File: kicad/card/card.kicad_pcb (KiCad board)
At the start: 2 copper layers, 30 x 34 mm, 6 parts, among them U1 RP2350_60QFN, U2 TLV70030_SOT23-5, U3 BNO086

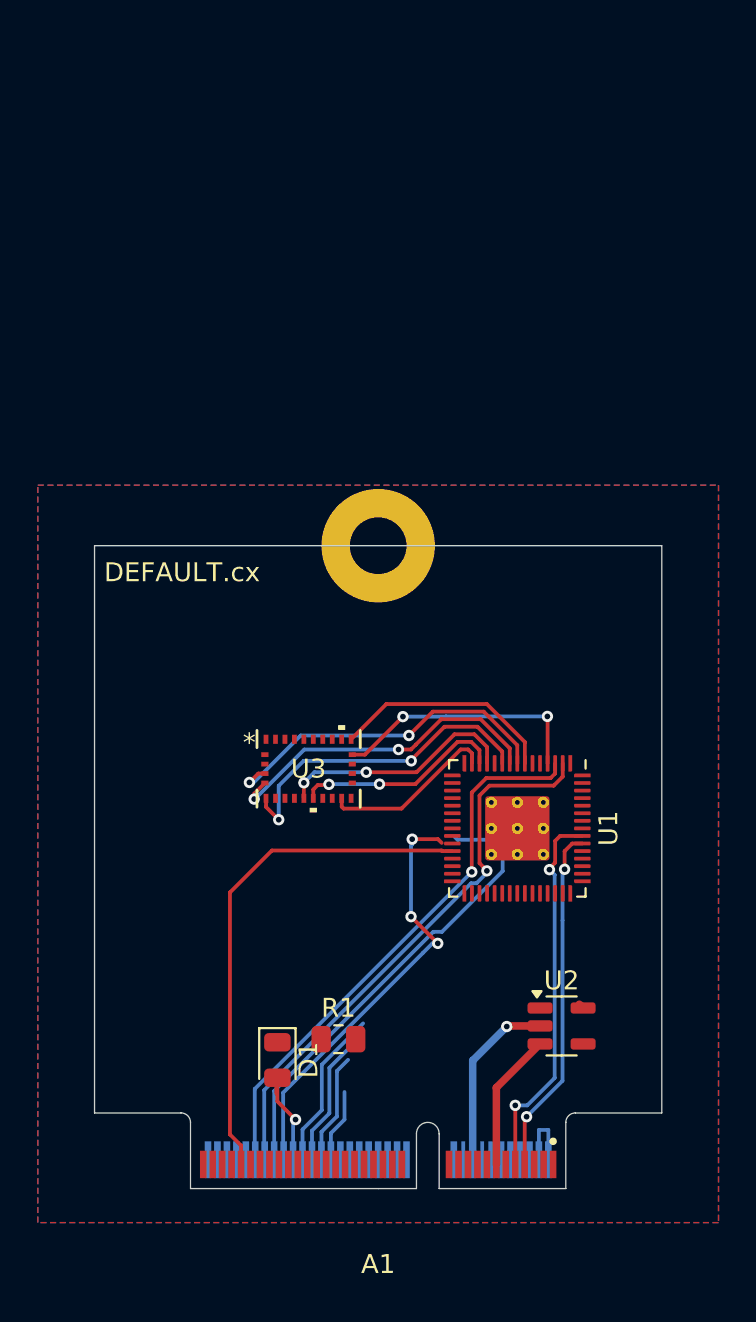
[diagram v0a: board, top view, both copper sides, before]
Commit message: minimal "blink" bring up revised schematic and starting with new components to place
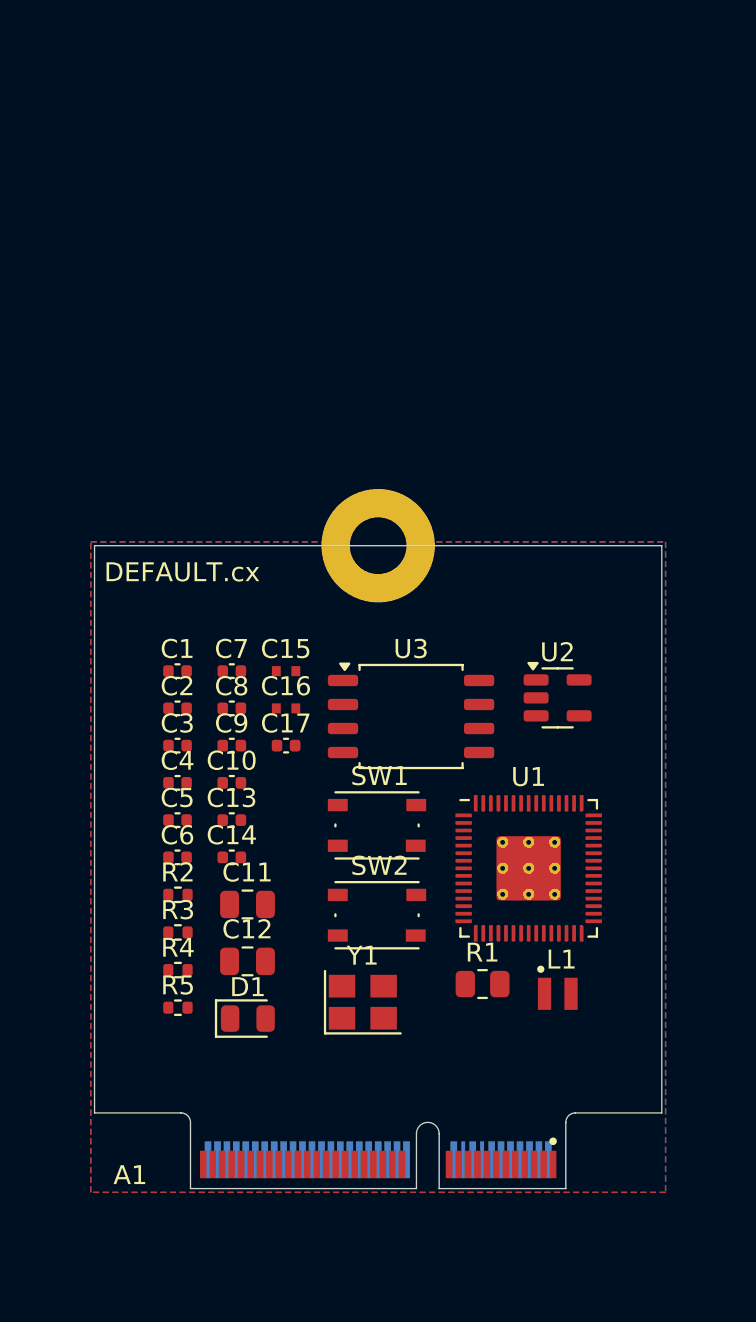
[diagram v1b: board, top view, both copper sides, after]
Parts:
- added C1: 100n, Capacitor_SMD:C_0402_1005Metric, F.Cu at (89.4, 104.8)
- added C10: 100n, Capacitor_SMD:C_0402_1005Metric, F.Cu at (92.3, 110.7)
- added C11: 10u, Capacitor_SMD:C_0805_2012Metric, F.Cu at (93.1, 117.2)
- added C12: 10u, Capacitor_SMD:C_0805_2012Metric, F.Cu at (93.1, 120.2)
- added C13: 15p, Capacitor_SMD:C_0402_1005Metric, F.Cu at (92.3, 112.7)
- added C14: 15p, Capacitor_SMD:C_0402_1005Metric, F.Cu at (92.3, 114.7)
- added C15: 4.7u, RP2350_60QFN_minimal:C_0402_1005Metric_small_pads, F.Cu at (95.1, 104.8)
- added C16: 4.7u, RP2350_60QFN_minimal:C_0402_1005Metric_small_pads, F.Cu at (95.1, 106.8)
- added C17: 4.7u, Capacitor_SMD:C_0402_1005Metric, F.Cu at (95.1, 108.8)
- added C2: 4.7u, Capacitor_SMD:C_0402_1005Metric, F.Cu at (89.4, 106.8)
- added C3: 100n, Capacitor_SMD:C_0402_1005Metric, F.Cu at (89.4, 108.8)
- added C4: 100n, Capacitor_SMD:C_0402_1005Metric, F.Cu at (89.4, 110.7)
- added C5: 100n, Capacitor_SMD:C_0402_1005Metric, F.Cu at (89.4, 112.7)
- added C6: 100n, Capacitor_SMD:C_0402_1005Metric, F.Cu at (89.4, 114.7)
- added C7: 100n, Capacitor_SMD:C_0402_1005Metric, F.Cu at (92.3, 104.8)
- added C8: 100n, Capacitor_SMD:C_0402_1005Metric, F.Cu at (92.3, 106.8)
- added C9: 100n, Capacitor_SMD:C_0402_1005Metric, F.Cu at (92.3, 108.8)
- added L1: 3.3u, RP2350_60QFN_minimal:L_pol_2016, F.Cu at (109.5, 121.9)
- added R2: 1k, Resistor_SMD:R_0402_1005Metric, F.Cu at (89.4, 116.7)
- added R3: 33, Resistor_SMD:R_0402_1005Metric, F.Cu at (89.4, 118.7)
- added R4: 1k, Resistor_SMD:R_0402_1005Metric, F.Cu at (89.4, 120.6)
- added R5: 1k, Resistor_SMD:R_0402_1005Metric, F.Cu at (89.4, 122.6)
- added SW1: SW_Push, Button_Switch_SMD:SW_Push_1P1T_NO_Vertical_Wuerth_434133025816, F.Cu at (99.9, 113.0)
- added SW2: SW_Push, Button_Switch_SMD:SW_Push_1P1T_NO_Vertical_Wuerth_434133025816, F.Cu at (99.9, 117.7)
- added Y1: ABM8-272-T3, Crystal:Crystal_SMD_3225-4Pin_3.2x2.5mm, F.Cu at (99.2, 122.3)
- U3: value BNO086 -> W25Q128JVS; footprint footprints:QFN28_BNO086_CEV -> Package_SO:SOIC-8_5.23x5.23mm_P1.27mm
- moved U2 17.4 mm to (109.5, 106.2)
- moved R1 8.16 mm to (105.5, 121.4)
- moved U3 6.09 mm to (101.7, 107.2)
- moved D1 2.69 mm to (93.1, 123.2), turned to 0 degrees
- moved U1 2.20 mm to (108.0, 115.3), turned to 0 degrees
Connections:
- D1 pad 1: Net-(D1-K) -> GND
- D1 pad 2: Net-(A1-TP90) -> Net-(D1-A)
- R1 pad 1: Net-(D1-K) -> Net-(A1-TP89)
- R1 pad 2: GND -> Net-(D1-A)
- U1 pad 1: unconnected-(U1-IOVDD-Pad1) -> +3V3
- U1 pad 10: Net-(U1-GPIO7) -> unconnected-(U1-GPIO7-Pad10)
- U1 pad 11: unconnected-(U1-IOVDD-Pad11) -> +3V3
- U1 pad 12: Net-(U1-GPIO8) -> unconnected-(U1-GPIO8-Pad12)
- U1 pad 13: Net-(U1-GPIO9) -> unconnected-(U1-GPIO9-Pad13)
- U1 pad 14: Net-(U1-GPIO10) -> unconnected-(U1-GPIO10-Pad14)
- U1 pad 15: Net-(A1-TP87) -> unconnected-(U1-GPIO11-Pad15)
- U1 pad 16: Net-(A1-TP88) -> unconnected-(U1-GPIO12-Pad16)
- U1 pad 17: Net-(A1-TP89) -> unconnected-(U1-GPIO13-Pad17)
- U1 pad 20: unconnected-(U1-IOVDD-Pad20) -> +3V3
- U1 pad 21: unconnected-(U1-XIN-Pad21) -> Net-(U1-XIN)
- U1 pad 22: unconnected-(U1-XOUT-Pad22) -> Net-(U1-XOUT)
- U1 pad 23: unconnected-(U1-DVDD-Pad23) -> +1V1
- U1 pad 24: Net-(A1-TP92) -> Net-(A1-TP85)
- U1 pad 25: Net-(A1-TP91) -> Net-(A1-TP86)
- U1 pad 26: RESET -> Net-(A1-XIO_A)
- U1 pad 30: unconnected-(U1-IOVDD-Pad30) -> +3V3
- U1 pad 38: unconnected-(U1-IOVDD-Pad38) -> +3V3
- U1 pad 39: unconnected-(U1-DVDD-Pad39) -> +1V1
- U1 pad 4: Net-(U1-GPIO2) -> Net-(A1-TP92)
- U1 pad 41: unconnected-(U1-GPIO27_ADC1-Pad41) -> Net-(U1-GPIO27_ADC1)
- U1 pad 42: unconnected-(U1-GPIO28_ADC2-Pad42) -> Net-(A1-TP88)
- U1 pad 43: unconnected-(U1-GPIO29_ADC3-Pad43) -> Net-(A1-TP87)
- U1 pad 44: unconnected-(U1-ADC_AVDD-Pad44) -> +3V3
- U1 pad 45: unconnected-(U1-IOVDD-Pad45) -> +3V3
- U1 pad 46: +3.3V -> Net-(U1-VREG_AVDD)
- U1 pad 47: +3.3V -> GND
- U1 pad 48: +3.3V -> Net-(U1-VREG_LX)
- U1 pad 49: +3.3V -> +3V3
- U1 pad 5: Net-(U1-GPIO3) -> Net-(A1-TP91)
- U1 pad 50: +3.3V -> +1V1
- U1 pad 51: Net-(A1-USB_DM) -> Net-(U1-USB_DM)
- U1 pad 52: Net-(A1-USB_DP) -> Net-(U1-USB_DP)
- U1 pad 53: unconnected-(U1-USB_OTP_VDD-Pad53) -> +3V3
- U1 pad 54: unconnected-(U1-QSPI_IOVDD-Pad54) -> +3V3
- U1 pad 55: unconnected-(U1-QSPI_SD3-Pad55) -> Net-(U1-QSPI_SD3)
- U1 pad 56: unconnected-(U1-QSPI_SCLK-Pad56) -> Net-(U1-QSPI_SCLK)
- U1 pad 57: unconnected-(U1-QSPI_SD0-Pad57) -> Net-(U1-QSPI_SD0)
- U1 pad 58: unconnected-(U1-QSPI_SD2-Pad58) -> Net-(U1-QSPI_SD2)
- U1 pad 59: unconnected-(U1-QSPI_SD1-Pad59) -> Net-(U1-QSPI_SD1)
- U1 pad 6: unconnected-(U1-DVDD-Pad6) -> +1V1
- U1 pad 60: unconnected-(U1-QSPI_SS-Pad60) -> Net-(U1-QSPI_SS)
- U1 pad 7: Net-(U1-GPIO4) -> Net-(A1-TP90)
- U1 pad 8: Net-(U1-GPIO5) -> Net-(A1-TP89)
- U1 pad 9: Net-(U1-GPIO6) -> unconnected-(U1-GPIO6-Pad9)
- U2 pad 1: +5V -> Net-(JP1-B)
- U2 pad 2: GND -> Net-(U2-GND)
- U2 pad 3: +5V -> Net-(JP1-B)
- U3 pad 1: unconnected-(U3-RESV_NC-Pad1) -> Net-(U1-QSPI_SS)
- U3 pad 2: unconnected-(U3-GND-Pad2) -> Net-(U1-QSPI_SD1)
- U3 pad 3: unconnected-(U3-VDD-Pad3) -> Net-(U1-QSPI_SD2)
- U3 pad 4: Net-(U1-GPIO5) -> GND
- U3 pad 5: Net-(U1-GPIO6) -> Net-(U1-QSPI_SD0)
- U3 pad 6: Net-(U1-GPIO7) -> Net-(U1-QSPI_SCLK)
- U3 pad 7: unconnected-(U3-RESV_NC-Pad7) -> Net-(U1-QSPI_SD3)
- U3 pad 8: unconnected-(U3-RESV_NC-Pad8) -> +3V3
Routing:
- net Net-(A1-UART_TX): track 30.3 -> 0.00 mm, vias 1 -> 0
- net Net-(A1-UART_RX): track 29.2 -> 0.00 mm, vias 1 -> 0
- net RESET: track 27.3 -> 0.00 mm
- net Net-(A1-TP92): track 24.5 -> 0.00 mm
- net Net-(A1-TP91): track 22.8 -> 0.00 mm, vias 3 -> 0
- net Net-(A1-USB_DP): track 20.1 -> 0.00 mm, vias 2 -> 0
- net Net-(U1-GPIO5): track 18.6 -> 0.00 mm, vias 2 -> 0
- net Net-(A1-USB_DM): track 18.6 -> 0.00 mm, vias 2 -> 0
- net Net-(U1-GPIO6): track 17.8 -> 0.00 mm, vias 2 -> 0
- net Net-(U1-GPIO7): track 17.7 -> 0.00 mm, vias 2 -> 0
- net Net-(A1-TP90): track 14.2 -> 0.00 mm, vias 1 -> 0
- net Net-(U1-GPIO2): track 13.6 -> 0.00 mm, vias 2 -> 0
- net Net-(U1-GPIO8): track 12.7 -> 0.00 mm, vias 2 -> 0
- net Net-(U1-GPIO4): track 11.9 -> 0.00 mm
- net Net-(U1-GPIO9): track 11.3 -> 0.00 mm, vias 2 -> 0
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
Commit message: compentents positioned in lower half of PCB
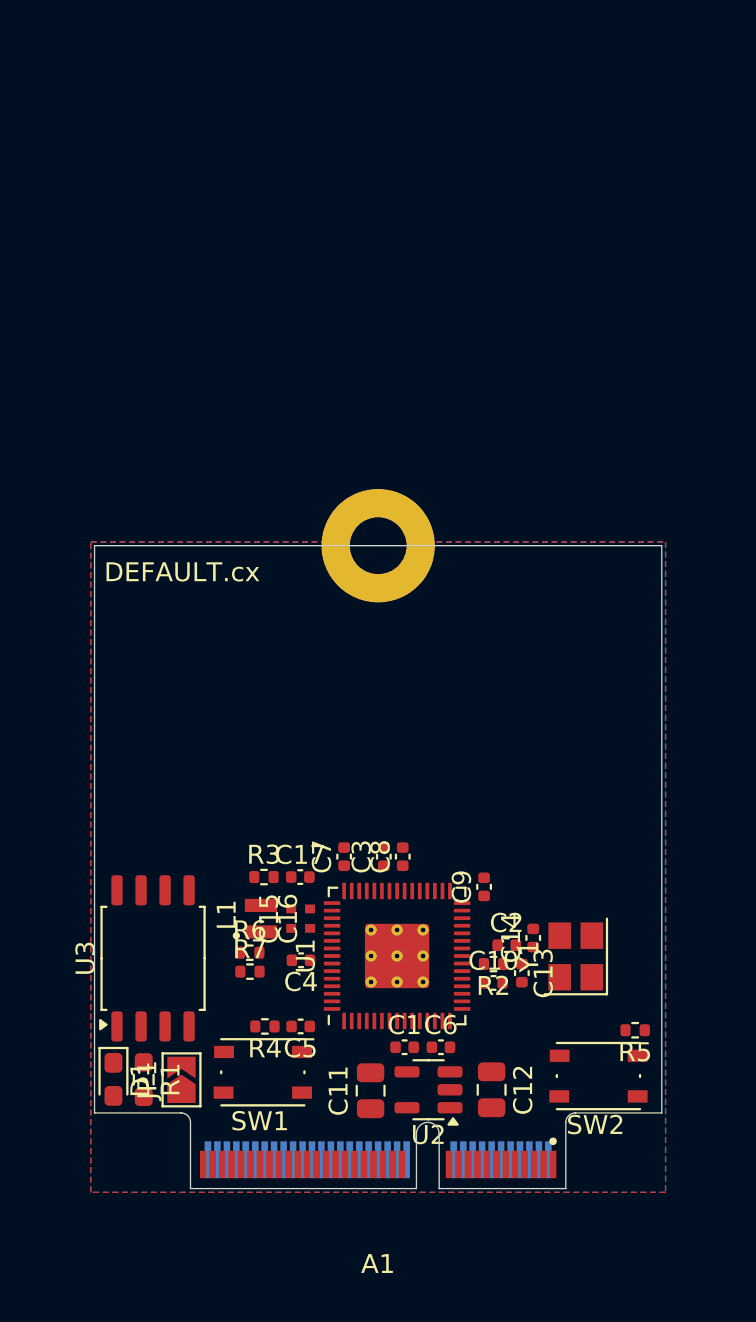
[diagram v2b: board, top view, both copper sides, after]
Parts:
- added JP1: Alt 5v, Jumper:SolderJumper-2_P1.3mm_Open_TrianglePad1.0x1.5mm, F.Cu at (89.6, 126.5)
- added R6: 27Ω, Resistor_SMD:R_0402_1005Metric, F.Cu at (93.2, 119.7)
- added R7: 27Ω, Resistor_SMD:R_0402_1005Metric, F.Cu at (93.2, 120.7)
- D1: footprint LED_SMD:LED_0805_2012Metric -> LED_SMD:LED_0603_1608Metric_Pad1.05x0.95mm_HandSolder
- R1: footprint Resistor_SMD:R_0805_2012Metric -> Resistor_SMD:R_0603_1608Metric_Pad0.98x0.95mm_HandSolder
- SW1: value SW_Push -> USB_BOOT
- SW2: value SW_Push -> RESET
- U1: value RP2350_60QFN -> RP2350A
- U3: value W25Q128JVS -> W25Q128
- Y1: value ABM8-272-T3 -> 12MHz
- moved R5 24.2 mm to (113.6, 123.8), turned to 180 degrees
- moved C1 23.2 mm to (101.4, 124.7)
- moved U2 21.8 mm to (102.7, 127.0), turned to 180 degrees
- moved C2 21.4 mm to (106.8, 119.3)
- moved U3 18.7 mm to (88.1, 120.0), turned to 90 degrees
- moved R1 18.6 mm to (87.6, 126.4), turned to -90 degrees
- moved C10 17.4 mm to (106.1, 121.3)
- moved C13 17.3 mm to (107.6, 120.8), turned to -90 degrees
- moved C6 17.2 mm to (103.3, 124.7)
- moved R2 17.1 mm to (106.1, 120.3), turned to 180 degrees
- moved C14 16.5 mm to (108.2, 118.9), turned to 90 degrees
- moved L1 16.2 mm to (93.8, 117.9), turned to 90 degrees
- moved C9 15.3 mm to (105.6, 116.2), turned to 90 degrees
- moved C12 14.6 mm to (106.0, 127.0), turned to -90 degrees
- moved SW2 14.5 mm to (111.7, 126.2), turned to 180 degrees
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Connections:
- A1 pad 13: +5V -> Net-(JP1-B)
- A1 pad 18: GND -> unconnected-(A1-GND-Pad18)
- A1 pad 2: +3.3V -> Net-(U1-GPIO27_ADC1)
- A1 pad 38: unconnected-(A1-TP85-Pad38) -> Net-(A1-TP85)
- A1 pad 4: +3.3V -> Net-(U1-GPIO27_ADC1)
- A1 pad 46: unconnected-(A1-TP86-Pad46) -> Net-(A1-TP86)
- A1 pad 52: Net-(A1-TP89) -> unconnected-(A1-TP89-Pad52)
- A1 pad 54: Net-(A1-TP90) -> Net-(A1-XIO_B)
- A1 pad 67: RESET -> Net-(A1-XIO_A)
- A1 pad 68: +5V -> Net-(JP1-A)
- A1 pad 70: +5V -> Net-(JP1-A)
- A1 pad 71: GND -> Net-(A1-GND-Pad71)
- A1 pad 72: +5V -> Net-(JP1-A)
- A1 pad 73: GND -> Net-(A1-GND-Pad71)
- R1 pad 1: Net-(A1-TP89) -> Net-(A1-XIO_B)
- U1 pad 8: Net-(A1-TP89) -> Net-(A1-XIO_B)

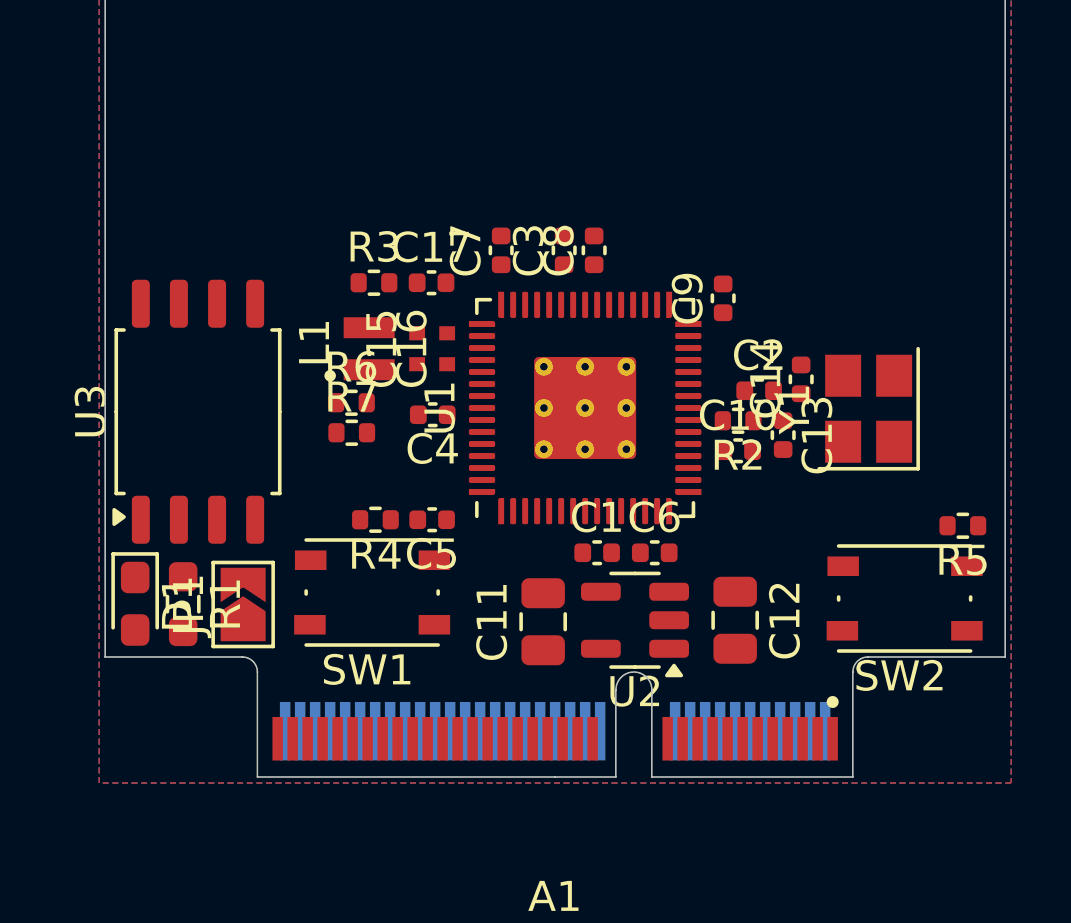
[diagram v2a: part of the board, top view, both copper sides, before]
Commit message: mostly routed, USB & +5V alt?
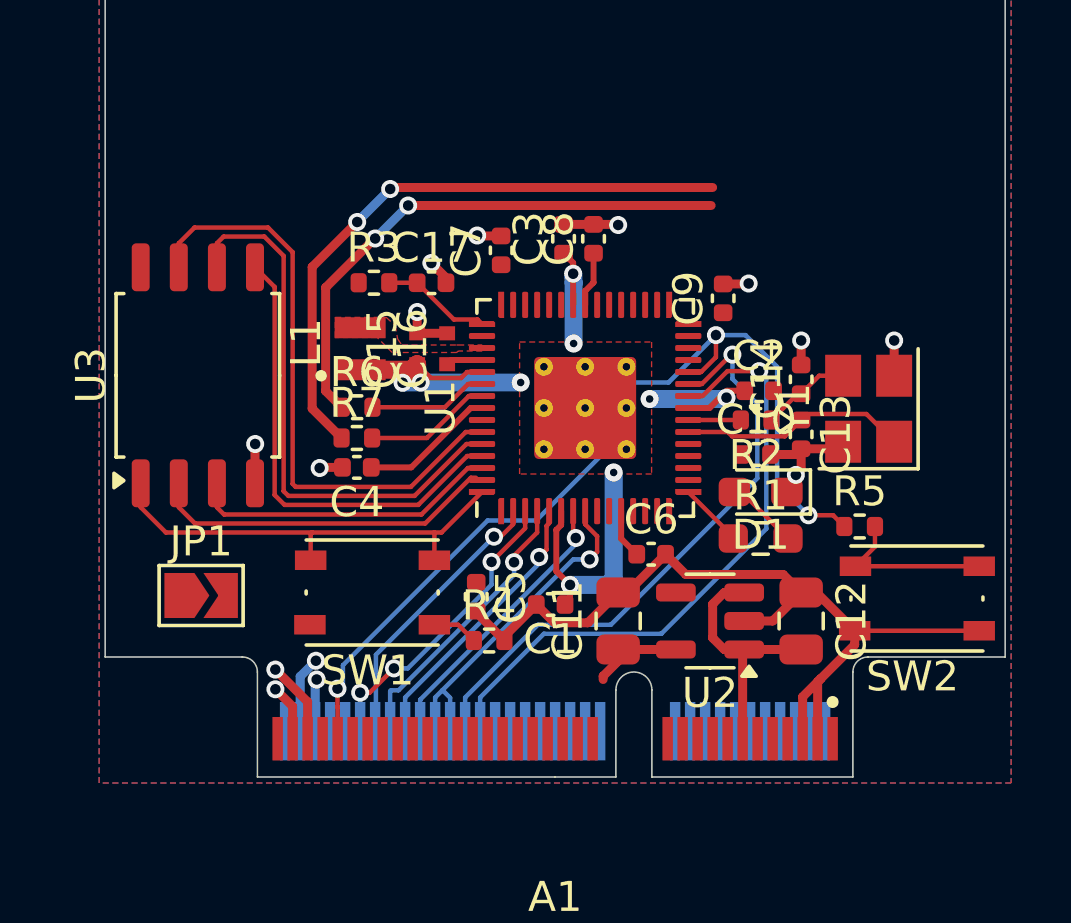
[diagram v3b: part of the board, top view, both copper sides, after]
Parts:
- moved D1 21.2 mm to (106.8, 122.7), turned to 180 degrees
- moved R1 19.4 mm to (106.8, 124.2), turned to 0 degrees
- moved R4 5.53 mm to (97.8, 127.7), turned to 0 degrees
- moved R5 3.44 mm to (110.2, 123.8), turned to 0 degrees
- moved C4 3.08 mm to (93.4, 121.9)
- moved C5 2.96 mm to (97.4, 126.2), turned to -90 degrees
- moved C11 2.50 mm to (102.1, 127.0)
- moved U2 2.50 mm to (105.2, 127.0)
- moved C1 2.32 mm to (99.8, 126.5), turned to 180 degrees
- moved C12 2.20 mm to (108.2, 127.0)
- moved JP1 1.43 mm to (88.2, 126.2), turned to 0 degrees
- moved U3 1.22 mm to (88.1, 118.8)
- moved C10 0.61 mm to (106.7, 121.5)
- moved C13 0.60 mm to (108.2, 120.8)
- moved R2 0.60 mm to (106.7, 120.3)
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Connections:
- net Net-(U1-VREG_LX) renamed /VREG_LX
- A1 pad 52: unconnected-(A1-TP89-Pad52) -> Net-(A1-TP89)
- A1 pad 54: Net-(A1-XIO_B) -> Net-(A1-TP89)
- A1 pad 71: Net-(A1-GND-Pad71) -> GND
- A1 pad 73: Net-(A1-GND-Pad71) -> GND
- C11 pad 1: +3.3V -> +3V3
- C11 pad 2: Net-(A1-GND-Pad71) -> GND
- C12 pad 1: Net-(U2-GND) -> GND
- R1 pad 1: Net-(A1-XIO_B) -> Net-(U1-GPIO12)
- R4 pad 1: Net-(U1-QSPI_SS) -> Net-(R4-Pad1)
- R4 pad 2: /~{USB_BOOT} -> GND
- R5 pad 1: Net-(R5-Pad1) -> Net-(A1-XIO_A)
- R5 pad 2: GND -> Net-(R5-Pad2)
- R7 pad 1: Net-(U1-USB_DP) -> Net-(A1-USB_DP)
- R7 pad 2: Net-(A1-USB_DP) -> Net-(U1-USB_DP)
- SW1 pad 1: GND -> Net-(R4-Pad1)
- SW2 pad 1: Net-(R5-Pad1) -> GND
- SW2 pad 2: Net-(A1-XIO_A) -> Net-(R5-Pad2)
- U1 pad 16: unconnected-(U1-GPIO12-Pad16) -> Net-(U1-GPIO12)
- U1 pad 24: Net-(A1-TP85) -> Net-(A1-TP87)
- U1 pad 25: Net-(A1-TP86) -> Net-(A1-TP88)
- U1 pad 42: Net-(A1-TP88) -> Net-(A1-TP86)
- U1 pad 43: Net-(A1-TP87) -> Net-(A1-TP85)
- U1 pad 60: Net-(U1-QSPI_SS) -> /~{USB_BOOT}
- U1 pad 8: Net-(A1-XIO_B) -> Net-(A1-TP89)
- U2 pad 2: Net-(U2-GND) -> GND
- U2 pad 5: +3.3V -> +3V3
- U3 pad 1: Net-(U1-QSPI_SS) -> /~{USB_BOOT}
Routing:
- net GND: track 0.00 -> 47.0 mm, vias 0 -> 12
- net Net-(A1-XIO_A): track 0.00 -> 31.5 mm, vias 0 -> 3
- net +1V1: track 0.00 -> 26.2 mm, vias 0 -> 9
- net Net-(A1-TP87): track 0.00 -> 21.1 mm, vias 0 -> 1
- net Net-(A1-USB_DP): track 0.00 -> 20.6 mm, vias 0 -> 2
- net Net-(A1-TP88): track 0.00 -> 20.2 mm, vias 0 -> 1
- net Net-(U1-QSPI_SD3): track 0.00 -> 20.0 mm
- net Net-(U1-QSPI_SCLK): track 0.00 -> 18.6 mm
- net Net-(A1-USB_DM): track 0.00 -> 18.2 mm, vias 0 -> 2
- net Net-(U1-QSPI_SD0): track 0.00 -> 15.7 mm
- net /~{USB_BOOT}: track 0.00 -> 15.0 mm
- net +3V3: track 0.00 -> 12.4 mm
- net Net-(U1-QSPI_SD1): track 0.00 -> 11.6 mm
- net Net-(A1-TP89): track 0.00 -> 11.5 mm, vias 0 -> 1
- net Net-(U1-QSPI_SD2): track 0.00 -> 10.4 mm
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- added copper zone on F.Cu, net +1V1
- added copper zone on F.Cu, net +3V3
- added copper zone on F.Cu, net /VREG_LX
- removed copper zone on F.Cu, net GND
